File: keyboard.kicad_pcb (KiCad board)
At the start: 2 copper layers, 333.4 x 114.3 mm, 192 parts, among them SW1 SW_Push, U1 ATmega32U4-AU, Y1 16MHz

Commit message: Connected rows to MCU
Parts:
- moved R3 29.5 mm to (265.9, 84.8)
- moved C5 5.83 mm to (260.2, 103.2)
- moved C7 3.90 mm to (241.3, 90.3), turned to 270 degrees
- moved C2 3.39 mm to (241.3, 86.7)
- moved Y1 2.37 mm to (252.9, 81.8)
- moved C4 2.28 mm to (258.0, 81.9)
- moved C1 2.25 mm to (263.0, 88.7)
- moved C3 2.25 mm to (247.0, 82.0)
- moved C6 2.25 mm to (242.0, 98.1)
- moved U1 2.25 mm to (252.9, 92.6)
- moved R4 2.25 mm to (263.2, 97.6)
- moved D56 0.86 mm to (198.4, 57.1)
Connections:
- U1 pad 10: Net-(U1-Pad10) -> COL2
- U1 pad 11: Net-(U1-Pad11) -> COL3
- U1 pad 12: Net-(U1-Pad12) -> COL7
- U1 pad 18: Net-(U1-Pad18) -> COL10
- U1 pad 19: Net-(U1-Pad19) -> COL11
- U1 pad 20: Net-(U1-Pad20) -> COL12
- U1 pad 21: Net-(U1-Pad21) -> COL13
- U1 pad 22: Net-(U1-Pad22) -> COL15
- U1 pad 25: Net-(U1-Pad25) -> COL14
- U1 pad 26: Net-(U1-Pad26) -> COL16
- U1 pad 28: Net-(U1-Pad28) -> COL4
- U1 pad 29: Net-(U1-Pad29) -> COL5
- U1 pad 30: Net-(U1-Pad30) -> COL6
- U1 pad 31: Net-(U1-Pad31) -> COL8
- U1 pad 32: Net-(U1-Pad32) -> COL9
- U1 pad 36: Net-(U1-Pad36) -> ROW5
- U1 pad 37: Net-(U1-Pad37) -> ROW4
- U1 pad 38: Net-(U1-Pad38) -> ROW3
- U1 pad 39: Net-(U1-Pad39) -> ROW2
- U1 pad 40: Net-(U1-Pad40) -> ROW1
- U1 pad 41: Net-(U1-Pad41) -> ROW0
- U1 pad 8: Net-(U1-Pad8) -> COL0
- U1 pad 9: Net-(U1-Pad9) -> COL1
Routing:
- net ROW1: track 0.00 -> 425.2 mm, vias 0 -> 2
- net ROW0: track 0.00 -> 423.7 mm, vias 0 -> 3
- net ROW2: track 0.00 -> 408.4 mm, vias 0 -> 2
- net ROW3: track 0.00 -> 398.2 mm, vias 0 -> 2
- net ROW4: track 0.00 -> 339.4 mm
- net ROW5: track 0.00 -> 299.3 mm
- net +5V: track 117.2 -> 0.00 mm, vias 1 -> 0
- net Net-(R1-Pad1): track 116.0 -> 0.00 mm
- net Net-(R2-Pad1): track 114.5 -> 0.00 mm
- net GND: track 44.4 -> 0.00 mm
- net Net-(C3-Pad1): track 26.0 -> 0.00 mm
- net Net-(C4-Pad1): track 8.92 -> 0.00 mm
- net Net-(R4-Pad2): track 4.59 -> 0.00 mm
- net VCC: track 3.55 -> 0.00 mm

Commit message: Connected some columns and crystal
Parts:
- moved C3 10.2 mm to (257.2, 81.9), turned to 90 degrees
- moved C4 9.53 mm to (248.4, 81.9), turned to 270 degrees
- turned Y1 to 180 degrees
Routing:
- net COL4: track 0.00 -> 342.0 mm, vias 0 -> 2
- net COL0: track 0.00 -> 334.4 mm, vias 0 -> 2
- net COL1: track 0.00 -> 321.5 mm, vias 0 -> 3
- net COL3: track 0.00 -> 317.3 mm, vias 0 -> 3
- net COL6: track 0.00 -> 307.9 mm, vias 0 -> 3
- net COL2: track 0.00 -> 294.6 mm, vias 0 -> 3
- net COL5: track 0.00 -> 291.9 mm, vias 0 -> 3
- net COL8: track 0.00 -> 252.2 mm, vias 0 -> 3
- net COL9: track 0.00 -> 237.1 mm, vias 0 -> 3
- net COL7: track 0.00 -> 202.2 mm, vias 0 -> 3
- net GND: track 0.00 -> 11.9 mm
- net Net-(C4-Pad1): track 0.00 -> 10.4 mm
- net Net-(C3-Pad1): track 0.00 -> 7.97 mm
- net Net-(D26-Pad2): track 0.00 -> 6.64 mm
- net Net-(D24-Pad2): track 0.00 -> 6.64 mm
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
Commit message: More traces
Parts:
- moved C6 25.7 mm to (265.9, 88.8), turned to 90 degrees
- moved C1 23.5 mm to (241.3, 97.8), turned to 270 degrees
- moved C2 14.7 mm to (245.3, 100.8), turned to 270 degrees
- moved C7 3.27 mm to (240.5, 93.5)
- moved C5 1.45 mm to (260.4, 101.7), turned to 270 degrees
- moved R4 0.97 mm to (263.2, 98.6)
- moved SW1 0.33 mm to (315.8, 74.1)
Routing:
- net COL16: track 0.00 -> 156.7 mm
- net COL15: track 0.00 -> 141.1 mm
- net COL13: track 0.00 -> 124.4 mm, vias 0 -> 3
- net COL14: track 0.00 -> 105.5 mm, vias 0 -> 1
- net GND: track 11.9 -> 115.1 mm, vias 0 -> 2
- net Net-(R3-Pad1): track 0.00 -> 68.7 mm, vias 0 -> 2
- net +5V: track 0.00 -> 58.9 mm, vias 0 -> 5
- net COL9: track 237.1 -> 258.2 mm
- net Net-(C7-Pad1): track 0.00 -> 6.74 mm
- net COL4: track 342.0 -> 336.6 mm
- net Net-(R4-Pad2): track 0.00 -> 5.30 mm
- net ROW5: track 299.3 -> 302.5 mm
- net COL10: track 0.00 -> 2.13 mm, vias 0 -> 1
- net ROW1: track 425.2 -> 426.6 mm

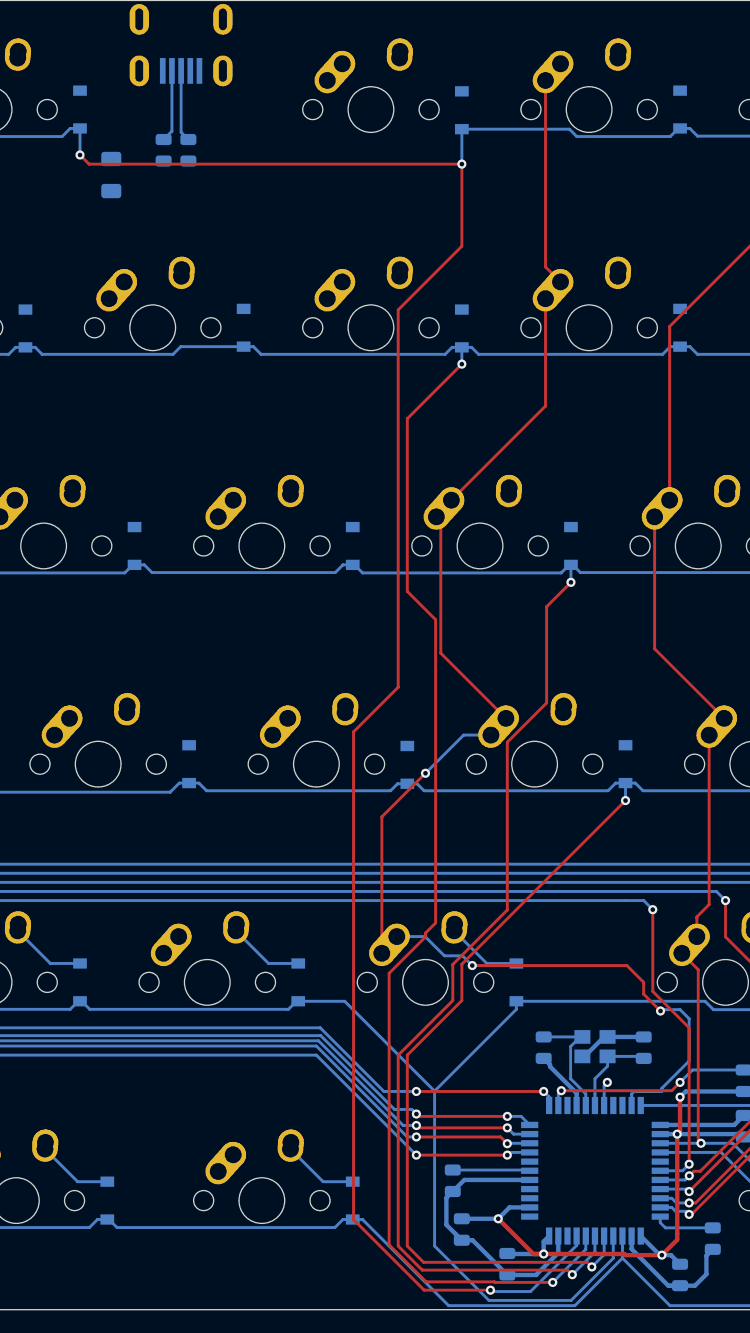
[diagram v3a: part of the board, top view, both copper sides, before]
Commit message: Connected usb to MCU
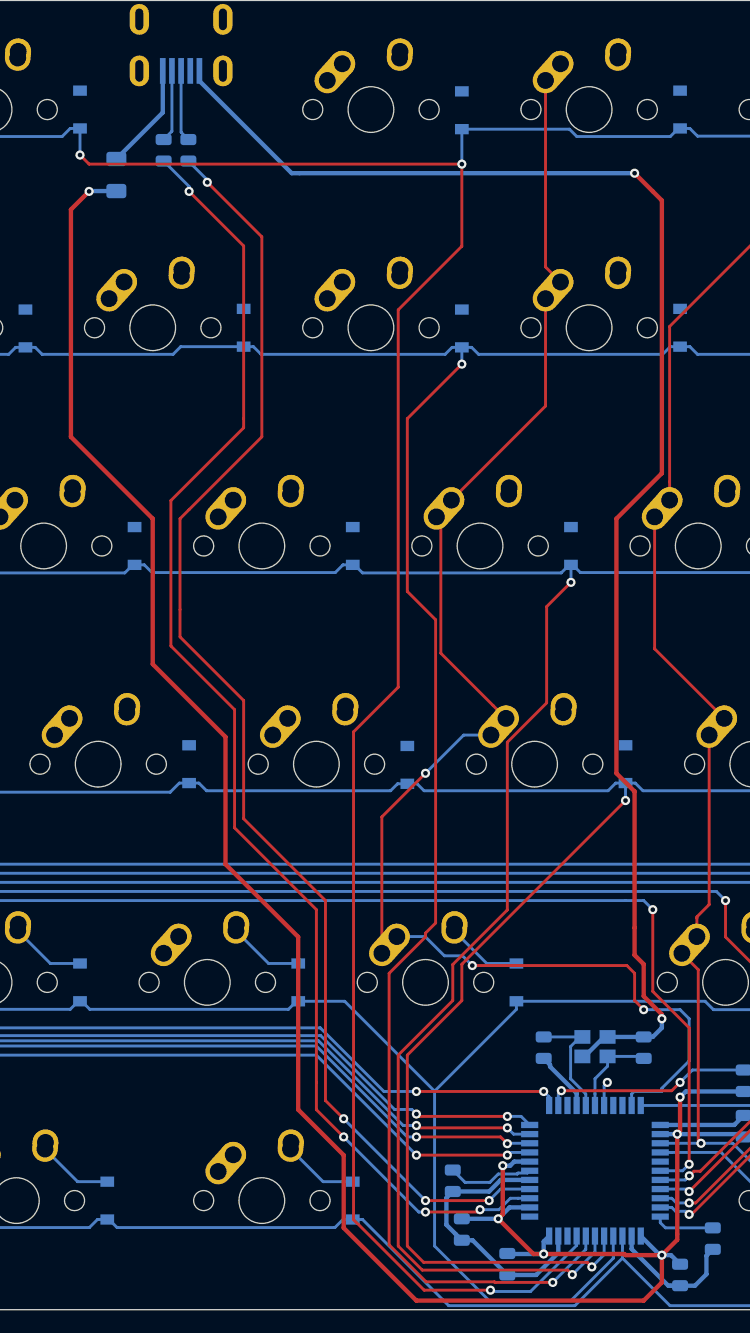
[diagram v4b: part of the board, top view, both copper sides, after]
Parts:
- moved F1 0.44 mm to (211.1, 5.71)
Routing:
- net +5V: track 58.9 -> 203.1 mm, vias 5 -> 7
- net GND: track 115.1 -> 238.1 mm, vias 2 -> 4
- net Net-(R1-Pad1): track 0.00 -> 116.4 mm, vias 0 -> 4
- net Net-(R2-Pad1): track 0.00 -> 114.8 mm, vias 0 -> 4
- net VCC: track 0.00 -> 9.37 mm
- net Net-(C7-Pad1): track 6.74 -> 7.59 mm
- net COL13: track 124.4 -> 125.1 mm

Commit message: All connected except gnd
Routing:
- net COL11: track 0.00 -> 175.0 mm, vias 0 -> 4
- net COL12: track 0.00 -> 172.8 mm, vias 0 -> 5
- net COL10: track 2.13 -> 174.4 mm, vias 1 -> 2
- net Net-(D81-Pad2): track 0.00 -> 15.5 mm
- net +5V: track 203.1 -> 217.3 mm
- net Net-(D41-Pad2): track 0.00 -> 7.03 mm
- net Net-(D7-Pad2): track 0.00 -> 7.03 mm
- net Net-(D33-Pad2): track 0.00 -> 7.03 mm
- net Net-(D32-Pad2): track 0.00 -> 7.03 mm
- net Net-(D17-Pad2): track 0.00 -> 7.03 mm
- net Net-(D77-Pad2): track 0.00 -> 7.03 mm
- net Net-(D2-Pad2): track 0.00 -> 7.03 mm
- net Net-(D79-Pad2): track 0.00 -> 7.03 mm
- net Net-(D46-Pad2): track 0.00 -> 7.03 mm
- net Net-(D86-Pad2): track 0.00 -> 7.03 mm
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
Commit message: Filled gnd zones
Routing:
- net GND: track 238.1 -> 290.1 mm
- net COL16: track 156.7 -> 161.9 mm
- added copper zone on B.Cu, net GND
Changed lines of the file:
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@@
     (thickness 1.6)
     (drawings 588)
-    (tracks 1394)
+    (tracks 1427)
     (zones 0)
     (modules 192)
@@
     (solder_mask_min_width 0.25)
     (aux_axis_origin 0 0)
-    (visible_elements FEFDEF7F)
+    (visible_elements FEFDFF7F)
     (pcbplotparams
       (layerselection 0x010fc_ffffffff)
@@
   (segment (start 243.68125 94.45625) (end 244.691 93.4465) (width 0.381) (layer B.Cu) (net 1))
   (segment (start 240.50625 94.45625) (end 243.68125 94.45625) (width 0.381) (layer B.Cu) (net 1))
+  (segment (start 247.887513 83.393737) (end 246.906237 83.393737) (width 0.381) (layer B.Cu) (net 1))
+  (segment (start 248.44375 82.8375) (end 247.887513 83.393737) (width 0.381) (layer B.Cu) (net 1))
+  (segment (start 246.906237 83.393737) (end 246.85625 83.34375) (width 0.381) (layer B.Cu) (net 1))
+  (segment (start 246.85625 80.95302) (end 248.43427 79.375) (width 0.381) (layer B.Cu) (net 1))
+  (segment (start 246.85625 83.34375) (end 246.85625 80.95302) (width 0.381) (layer B.Cu) (net 1))
+  (segment (start 253.9205 80.9625) (end 254.0205 80.9625) (width 0.381) (layer B.Cu) (net 1))
+  (segment (start 252.333 79.375) (end 253.9205 80.9625) (width 0.381) (layer B.Cu) (net 1))
+  (segment (start 248.43427 79.375) (end 252.333 79.375) (width 0.381) (layer B.Cu) (net 1))
+  (segment (start 251.3205 88.0775) (end 249.2375 90.1605) (width 0.381) (layer B.Cu) (net 1))
+  (segment (start 251.3205 86.9465) (end 251.3205 88.0775) (width 0.381) (layer B.Cu) (net 1))
+  (segment (start 248.3515 93.4465) (end 247.2205 93.4465) (width 0.381) (layer B.Cu) (net 1))
+  (segment (start 249.2375 92.5605) (end 248.3515 93.4465) (width 0.381) (layer B.Cu) (net 1))
+  (segment (start 249.2375 90.1605) (end 249.2375 92.5605) (width 0.381) (layer B.Cu) (net 1))
+  (segment (start 251.8895 88.6465) (end 258.6205 88.6465) (width 0.381) (layer B.Cu) (net 1))
+  (segment (start 251.3205 88.0775) (end 251.8895 88.6465) (width 0.381) (layer B.Cu) (net 1))
+  (segment (start 249.7205 98.3465) (end 249.7205 94.93925) (width 0.381) (layer B.Cu) (net 1))
+  (segment (start 248.3515 93.57025) (end 248.3515 93.4465) (width 0.381) (layer B.Cu) (net 1))
+  (segment (start 249.7205 94.93925) (end 248.3515 93.57025) (width 0.381) (layer B.Cu) (net 1))
+  (segment (start 253.84425 94.93925) (end 249.7205 94.93925) (width 0.381) (layer B.Cu) (net 1))
+  (segment (start 256.1205 97.2155) (end 253.84425 94.93925) (width 0.381) (layer B.Cu) (net 1))
+  (segment (start 256.1205 98.3465) (end 256.1205 97.2155) (width 0.381) (layer B.Cu) (net 1))
+  (segment (start 257.4895 88.6465) (end 258.6205 88.6465) (width 0.381) (layer B.Cu) (net 1))
+  (segment (start 253.84425 92.29175) (end 257.4895 88.6465) (width 0.381) (layer B.Cu) (net 1))
+  (segment (start 253.84425 94.93925) (end 253.84425 92.29175) (width 0.381) (layer B.Cu) (net 1))
   (segment (start 265.659 89.4465) (end 265.90625 89.69375) (width 0.381) (layer B.Cu) (net 2))
   (via (at 260.10275 89.4465) (size 0.8) (drill 0.4) (layers F.Cu B.Cu) (net 2))
@@
   (segment (start 310.515 -2.54) (end 310.515 13.74) (width 0.254) (layer F.Cu) (net 116))
   (segment (start 259.6245 91.0465) (end 258.6205 91.0465) (width 0.254) (layer B.Cu) (net 116))
-  (segment (start 263.937874 91.0465) (end 259.6245 91.0465) (width 0.254) (layer B.Cu) (net 116))
-  (segment (start 270.66875 92.075) (end 268.582359 94.161391) (width 0.254) (layer B.Cu) (net 116))
   (segment (start 272.438251 88.717999) (end 270.66875 90.4875) (width 0.254) (layer B.Cu) (net 116))
   (segment (start 277.630499 88.717999) (end 272.438251 88.717999) (width 0.254) (layer B.Cu) (net 116))
@@
   (segment (start 287.3375 94.45625) (end 287.3375 96.04375) (width 0.254) (layer B.Cu) (net 116))
   (segment (start 289.71875 90.4875) (end 289.71875 92.075) (width 0.254) (layer B.Cu) (net 116))
-  (segment (start 267.052765 94.161391) (end 263.937874 91.0465) (width 0.254) (layer B.Cu) (net 116))
-  (segment (start 268.582359 94.161391) (end 267.052765 94.161391) (width 0.254) (layer B.Cu) (net 116))
   (segment (start 283.36875 94.45625) (end 277.630499 88.717999) (width 0.254) (layer B.Cu) (net 116))
   (segment (start 286.54375 96.8375) (end 284.1625 96.8375) (width 0.254) (layer B.Cu) (net 116))
@@
   (segment (start 305.7525 92.71) (end 301.14875 88.10625) (width 0.254) (layer B.Cu) (net 116))
   (segment (start 292.1 88.10625) (end 289.71875 90.4875) (width 0.254) (layer B.Cu) (net 116))
+  (segment (start 261.191212 91.0465) (end 261.425962 91.28125) (width 0.254) (layer B.Cu) (net 116))
+  (segment (start 259.6245 91.0465) (end 261.191212 91.0465) (width 0.254) (layer B.Cu) (net 116))
+  (segment (start 261.425962 91.28125) (end 261.9375 91.28125) (width 0.254) (layer B.Cu) (net 116))
+  (segment (start 261.9375 91.28125) (end 264.31875 93.6625) (width 0.254) (layer B.Cu) (net 116))
+  (segment (start 264.31875 93.6625) (end 264.31875 96.04375) (width 0.254) (layer B.Cu) (net 116))
+  (segment (start 264.31875 96.04375) (end 265.1125 96.8375) (width 0.254) (layer B.Cu) (net 116))
+  (segment (start 265.1125 96.8375) (end 265.90625 97.63125) (width 0.254) (layer B.Cu) (net 116))
+  (segment (start 265.90625 97.63125) (end 266.7 97.63125) (width 0.254) (layer B.Cu) (net 116))
+  (segment (start 266.7 97.63125) (end 268.2875 96.04375) (width 0.254) (layer B.Cu) (net 116))
+  (segment (start 268.2875 96.04375) (end 268.2875 95.25) (width 0.254) (layer B.Cu) (net 116))
+  (segment (start 268.2875 95.25) (end 268.2875 94.45625) (width 0.254) (layer B.Cu) (net 116))
+  (segment (start 268.2875 94.45625) (end 269.08125 93.6625) (width 0.254) (layer B.Cu) (net 116))
+  (segment (start 269.08125 93.6625) (end 270.66875 92.075) (width 0.254) (layer B.Cu) (net 116))
   (via (at 245.26875 91.28125) (size 0.8) (drill 0.4) (layers F.Cu B.Cu) (net 117))
   (segment (start 245.5035 91.0465) (end 245.26875 91.28125) (width 0.254) (layer B.Cu) (net 117))
@@
   (segment (start 259.07625 97.63125) (end 258.6205 97.1755) (width 0.254) (layer B.Cu) (net 123))
   (segment (start 263.2075 97.63125) (end 259.07625 97.63125) (width 0.254) (layer B.Cu) (net 123))
+  (zone (net 1) (net_name GND) (layer B.Cu) (hatch full 0.508)
+    (connect_pads yes (clearance 0.508))
+    (min_thickness 0.254)
+    (fill yes (arc_segments 32) (thermal_gap 0.508) (thermal_bridge_width 0.508))
+    (polygon
+      (pts
+        (xy 247.30964 83.54314) (xy 247.2944 83.98002) (xy 245.26748 83.99526) (xy 245.38686 79.96682) (xy 246.71274 79.02194)
+        (xy 248.11736 78.46568) (xy 251.65304 78.17612) (xy 255.05918 78.16088) (xy 256.06502 79.75092) (xy 255.99898 80.137)
+        (xy 252.8062 80.05572) (xy 248.93778 80.01762) (xy 247.47982 80.12176) (xy 247.19026 80.1624) (xy 247.32234 83.09102)
+        (xy 247.32234 83.2358)
+      )
+    )
+  )
+  (zone (net 1) (net_name GND) (layer B.Cu) (hatch full 0.508)
+    (connect_pads yes (clearance 0.508))
+    (min_thickness 0.254)
+    (fill yes (arc_segments 32) (thermal_gap 0.508) (thermal_bridge_width 0.508))
+    (polygon
+      (pts
+        (xy 247.45442 80.23352) (xy 247.12422 80.43164) (xy 247.10898 80.0354) (xy 247.46712 79.98206) (xy 247.46712 80.23352)
+      )
+    )
+  )
+  (zone (net 1) (net_name GND) (layer B.Cu) (hatch full 0.508)
+    (priority 1)
+    (connect_pads yes (clearance 0.508))
+    (min_thickness 0.254)
+    (fill yes (arc_segments 32) (thermal_gap 0.508) (thermal_bridge_width 0.508))
+    (polygon
+      (pts
+        (xy 248.44375 88.10625) (xy 257.175 88.10625) (xy 257.175 96.8375) (xy 248.44375 96.8375)
+      )
+    )
+  )
 )

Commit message: Decoration
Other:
- board text added: "theKing"
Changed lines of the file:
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@@
   (general
     (thickness 1.6)
-    (drawings 588)
+    (drawings 589)
     (tracks 1427)
     (zones 0)
@@
     )
   )
+  (gr_text theKing (at 1.5875 100.0125) (layer F.SilkS)
+    (effects (font (size 3 3) (thickness 0.15)))
+  )
   (gr_line (start -9.525 102.362) (end -9.525 -7.112) (layer Edge.Cuts) (width 0.05))
